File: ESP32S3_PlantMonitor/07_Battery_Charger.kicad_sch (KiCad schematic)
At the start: 0 parts

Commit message: Continue battery charger schematic
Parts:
- added J3: Conn_01x02, symbol Connector_Generic:Conn_01x02
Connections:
- new net GND: J3.2 (Pin_2)
- new net VBAT_RAW: J3.1 (Pin_1)
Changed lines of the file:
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@@
 	(generator_version "10.0")
 	(paper "A4")
+	(wire
+		(pts
+			(xy 95.25 93.98) (xy 107.95 93.98)
+		)
+		(stroke
+			(width 0)
+			(type default)
+		)
+	)
+	(wire
+		(pts
+			(xy 95.25 96.52) (xy 107.95 96.52)
+		)
+		(stroke
+			(width 0)
+			(type default)
+		)
+	)
+	(global_label "VBAT_RAW"
+		(shape input)
+		(at 95.25 93.98 180)
+		(fields_autoplaced yes)
+		(effects
+			(font
+				(size 1.27 1.27)
+			)
+			(justify right)
+		)
+		(property "Intersheetrefs" "${INTERSHEET_REFS}"
+			(at 83.0724 93.98 0)
+			(hide yes)
+			(show_name no)
+			(do_not_autoplace no)
+			(effects
+				(font
+					(size 1.27 1.27)
+				)
+				(justify right)
+			)
+		)
+	)
+	(symbol
+		(lib_id "Connector_Generic:Conn_01x02")
+		(at 113.03 93.98 0)
+		(unit 1)
+		(body_style 1)
+		(exclude_from_sim no)
+		(in_bom yes)
+		(on_board yes)
+		(in_pos_files yes)
+		(dnp no)
+		(fields_autoplaced yes)
+		(property "Reference" "J3"
+			(at 115.57 93.9799 0)
+			(show_name no)
+			(do_not_autoplace no)
+			(effects
+				(font
+					(size 1.27 1.27)
+				)
+				(justify left)
+			)
+		)
+		(property "Value" "Conn_01x02"
+			(at 115.57 96.5199 0)
+			(show_name no)
+			(do_not_autoplace no)
+			(effects
+				(font
+					(size 1.27 1.27)
+				)
+				(justify left)
+			)
+		)
+		(property "Footprint" ""
+			(at 113.03 93.98 0)
+			(hide yes)
+			(show_name no)
+			(do_not_autoplace no)
+			(effects
+				(font
+					(size 1.27 1.27)
+				)
+			)
+		)
+		(property "Datasheet" ""
+			(at 113.03 93.98 0)
+			(hide yes)
+			(show_name no)
+			(do_not_autoplace no)
+			(effects
+				(font
+					(size 1.27 1.27)
+				)
+			)
+		)
+		(property "Description" "Generic connector, single row, 01x02, script generated (kicad-library-utils/schlib/autogen/connector/)"
+			(at 113.03 93.98 0)
+			(hide yes)
+			(show_name no)
+			(do_not_autoplace no)
+			(effects
+				(font
+					(size 1.27 1.27)
+				)
+			)
+		)
+		(pin "2"
+		)
+		(pin "1"
+		)
+		(instances
+			(project "ESP32S3_PlantMonitor"
+				(path "/02dfef50-593f-4b20-9f93-d1417ef98d67/c936da17-2809-47d6-8926-8fc850f8b85e"
+					(reference "J3")
+					(unit 1)
+				)
+			)
+		)
+	)
+	(symbol
+		(lib_id "power:GND")
+		(at 95.25 96.52 0)
+		(unit 1)
+		(body_style 1)
+		(exclude_from_sim no)
+		(in_bom yes)
+		(on_board yes)
+		(in_pos_files yes)
+		(dnp no)
+		(fields_autoplaced yes)
+		(property "Reference" "#PWR039"
+			(at 95.25 102.87 0)
+			(hide yes)
+			(show_name no)
+			(do_not_autoplace no)
+			(effects
+				(font
+					(size 1.27 1.27)
+				)
+			)
+		)
+		(property "Value" "GND"
+			(at 95.25 101.6 0)
+			(show_name no)
+			(do_not_autoplace no)
+			(effects
+				(font
+					(size 1.27 1.27)
+				)
+			)
+		)
+		(property "Footprint" ""
+			(at 95.25 96.52 0)
+			(hide yes)
+			(show_name no)
+			(do_not_autoplace no)
+			(effects
+				(font
+					(size 1.27 1.27)
+				)
+			)
+		)
+		(property "Datasheet" ""
+			(at 95.25 96.52 0)
+			(hide yes)
+			(show_name no)
+			(do_not_autoplace no)
+			(effects
+				(font
+					(size 1.27 1.27)
+				)
+			)
+		)
+		(property "Description" "Power symbol creates a global label with name \"GND\" , ground"
+			(at 95.25 96.52 0)
+			(hide yes)
+			(show_name no)
+			(do_not_autoplace no)
+			(effects
+				(font
+					(size 1.27 1.27)
+				)
+			)
+		)
+		(pin "1"
+		)
+		(instances
+			(project "ESP32S3_PlantMonitor"
+				(path "/02dfef50-593f-4b20-9f93-d1417ef98d67/c936da17-2809-47d6-8926-8fc850f8b85e"
+					(reference "#PWR039")
+					(unit 1)
+				)
+			)
+		)
+	)
 )

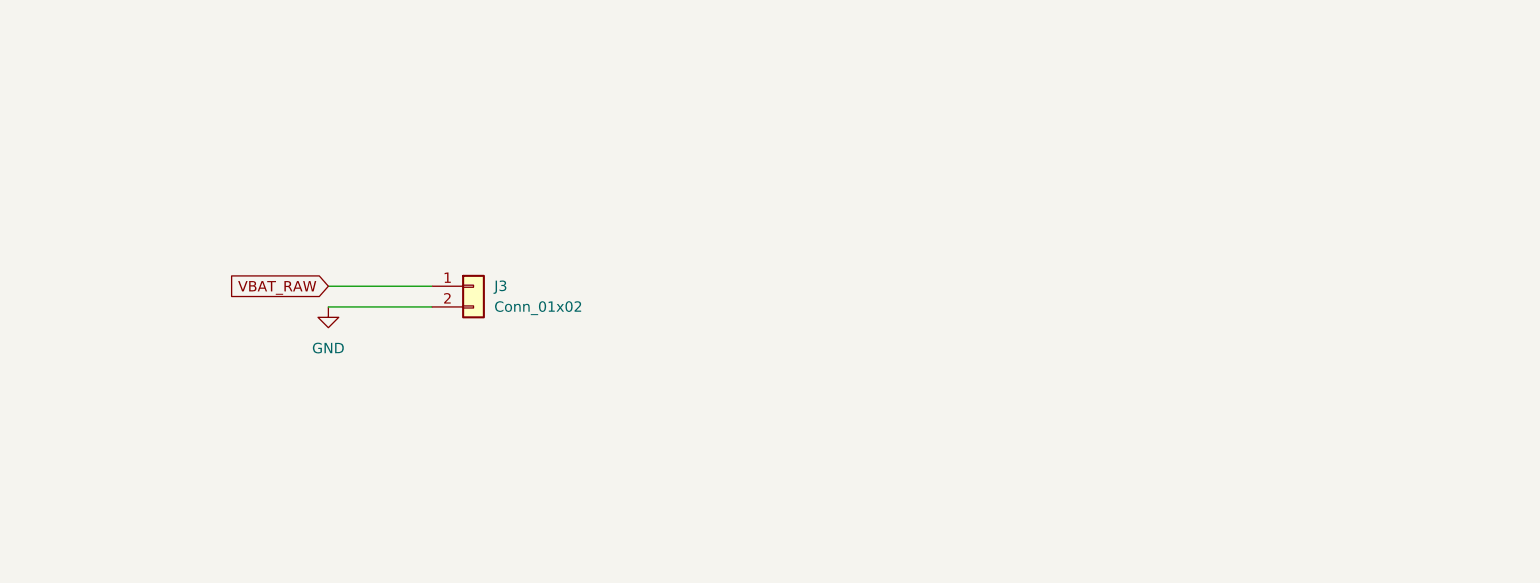
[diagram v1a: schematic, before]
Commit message: Complete battery charger schematic
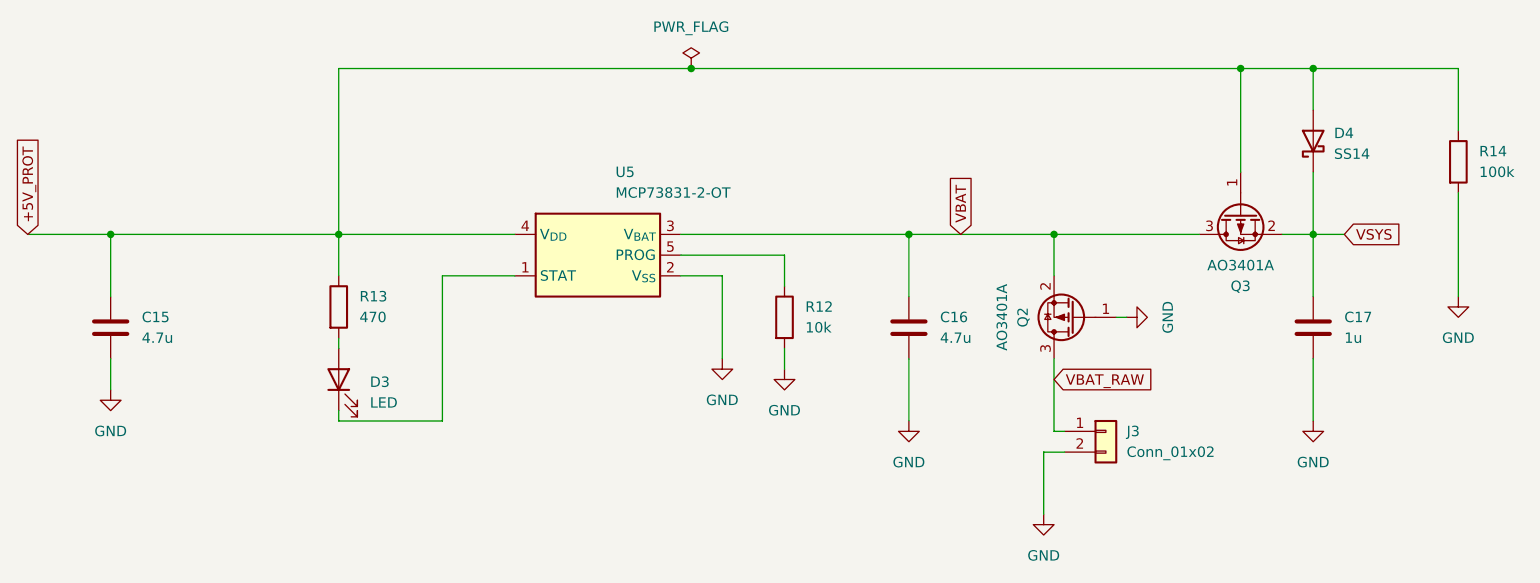
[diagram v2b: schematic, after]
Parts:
- added C15, C16: 4.7u, symbol Device:C
- added C17: 1u, symbol Device:C
- added D3: LED, symbol Device:LED
- added D4: SS14, Diode_SMD:D_SMA, symbol Diode:SS14
- added Q2, Q3: AO3401A, symbol Transistor_FET:Q_PMOS_GSD
- added R12: 10k, symbol Device:R
- added R13: 470, symbol Device:R
- added R14: 100k, symbol Device:R
- added U5: MCP73831-2-OT, Package_TO_SOT_SMD:SOT-23-5, symbol Battery_Management:MCP73831-2-OT
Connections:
- net GND: now also C15.2, C16.2, C17.2, Q2.1 (G), R12.2, R14.2, U5.2 (V_{SS})
- net VBAT_RAW: now also Q2.3 (D)
- new net: D3.1 (K), U5.1 (STAT)
- new net: D3.2 (A), R13.2
- new net: R12.1, U5.5 (PROG)
- new net +5V_PROT: C15.1, D4.2 (A), Q3.1 (G), R13.1, R14.1, U5.4 (V_{DD})
- new net VBAT: C16.1, Q2.2 (S), Q3.3 (D), U5.3 (V_{BAT})
- new net VSYS: C17.1, D4.1 (K), Q3.2 (S)
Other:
- moved on the sheet: J3
